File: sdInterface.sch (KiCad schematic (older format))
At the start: 3 parts, among them J1 SD_Card, J2 Conn_02x12_Counter_Clockwise

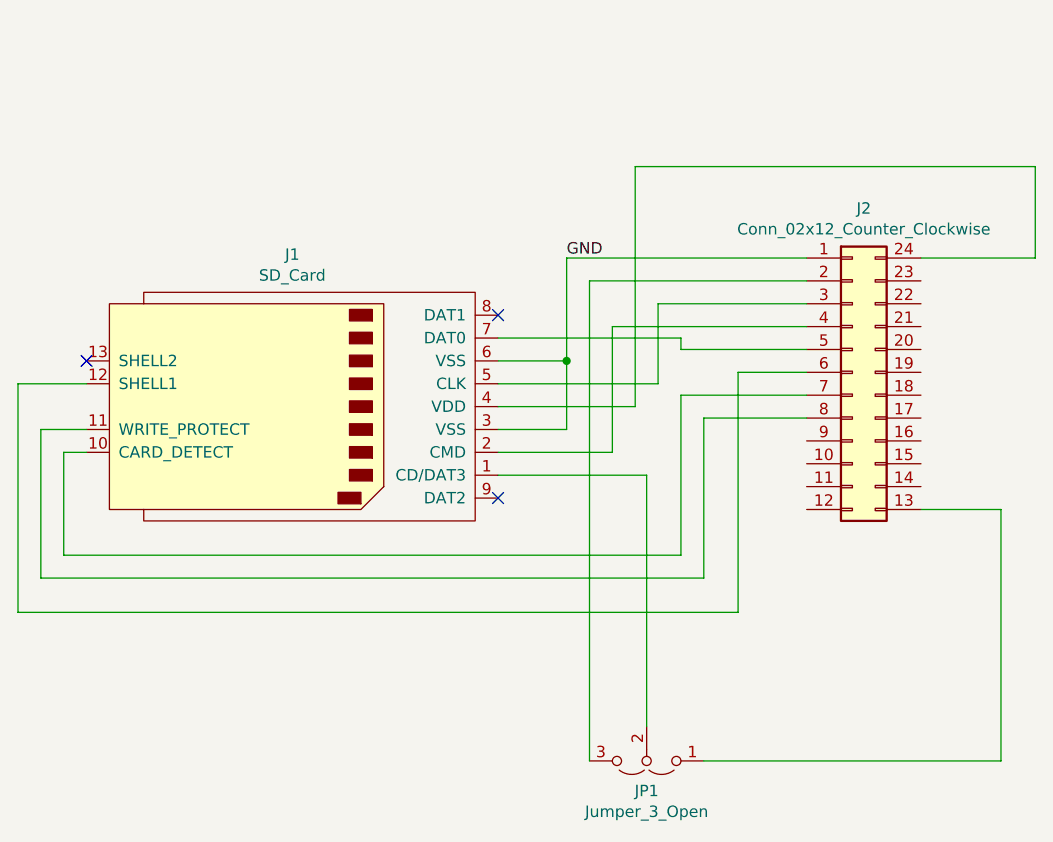
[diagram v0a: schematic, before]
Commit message: Added 3.3v reg, JP1 now pins
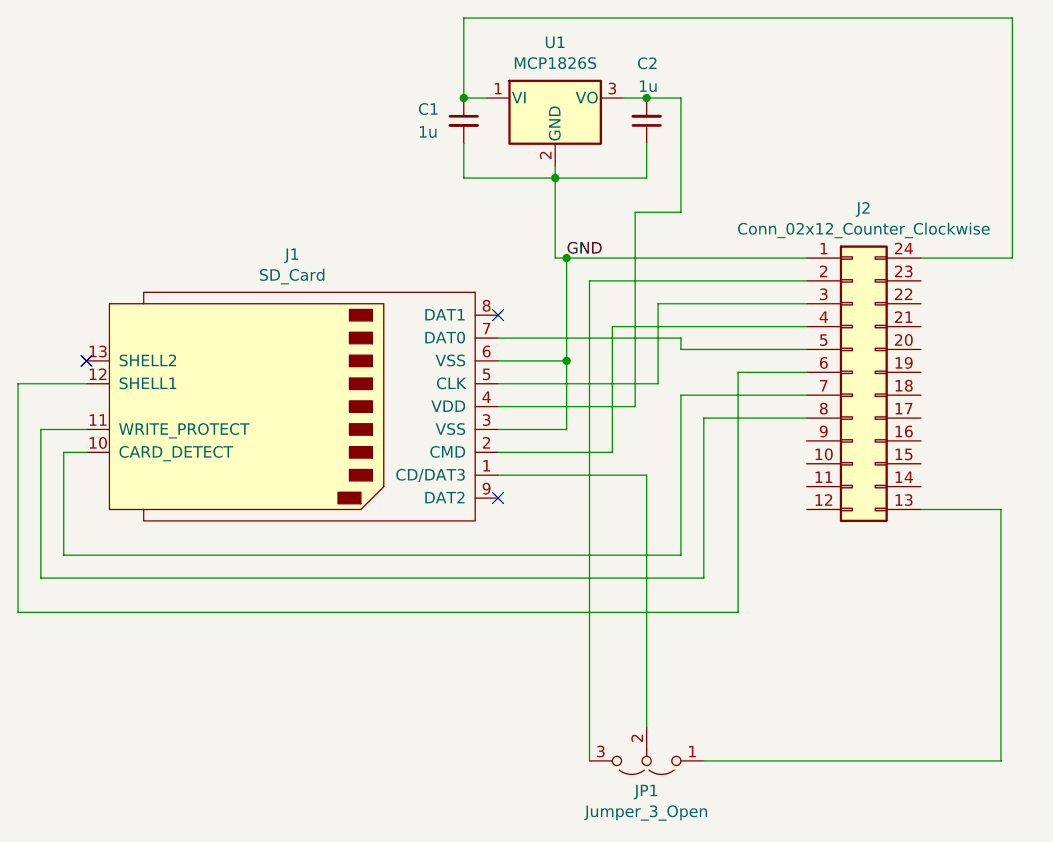
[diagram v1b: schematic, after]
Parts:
- added C1, C2: 1u, Capacitor_SMD:C_0805_2012Metric_Pad1.15x1.40mm_HandSolder, symbol Device:C_Small
- added U1: MCP1826S, Package_TO_SOT_SMD:SOT-223-3_TabPin2, symbol Regulator_Linear:MCP1826S
- JP1: footprint Jumper:SolderJumper-3_P1.3mm_Open_RoundedPad1.0x1.5mm -> Connector_PinHeader_2.54mm:PinHeader_1x03_P2.54mm_Vertical
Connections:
- net GND: now also C1.2, C2.1, U1.2 (GND)
- net at J2.24 (Pin_24): now also C1.1, U1.1 (VI); no longer J1.4 (VDD)
- new net: C2.2, J1.4 (VDD), U1.3 (VO)
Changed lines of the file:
@@
 F 0 "JP1" H 6150 5231 50  0000 C CNN
 F 1 "Jumper_3_Open" H 6150 5322 50  0000 C CNN
-F 2 "Jumper:SolderJumper-3_P1.3mm_Open_RoundedPad1.0x1.5mm" H 6150 5100 50  0001 C CNN
+F 2 "Connector_PinHeader_2.54mm:PinHeader_1x03_P2.54mm_Vertical" H 6150 5100 50  0001 C CNN
 F 3 "~" H 6150 5100 50  0001 C CNN
 	1    6150 5100
@@
 Wire Wire Line
 	5500 3550 6100 3550
-Wire Wire Line
-	6100 3550 6100 2500
-Wire Wire Line
-	6100 2500 7850 2500
-Wire Wire Line
-	7850 2500 7850 2900
-Wire Wire Line
-	7850 2900 7350 2900
 Wire Wire Line
 	5500 3450 6200 3450
@@
 Text Label 5800 2900 0    50   ~ 0
 GND
+$Comp
+L Regulator_Linear:MCP1826S U1
+U 1 1 5E2BFAF6
+P 5750 2200
+F 0 "U1" H 5750 2442 50  0000 C CNN
+F 1 "MCP1826S" H 5750 2351 50  0000 C CNN
+F 2 "Package_TO_SOT_SMD:SOT-223-3_TabPin2" H 5650 2350 50  0001 C CNN
+F 3 "http://ww1.microchip.com/downloads/en/DeviceDoc/22057B.pdf" H 5750 2450 50  0001 C CNN
+	1    5750 2200
+	1    0    0    -1
+$EndComp
+Wire Wire Line
+	5750 2500 5750 2550
+Wire Wire Line
+	5750 2900 5800 2900
+Connection ~ 5800 2900
+Wire Wire Line
+	7750 1850 7750 2900
+Wire Wire Line
+	7750 2900 7350 2900
+$Comp
+L Device:C_Small C1
+U 1 1 5E2C5E59
+P 5350 2300
+F 0 "C1" H 5150 2350 50  0000 L CNN
+F 1 "1u" H 5150 2250 50  0000 L CNN
+F 2 "Capacitor_SMD:C_0805_2012Metric_Pad1.15x1.40mm_HandSolder" H 5350 2300 50  0001 C CNN
+F 3 "~" H 5350 2300 50  0001 C CNN
+	1    5350 2300
+	1    0    0    -1
+$EndComp
+$Comp
+L Device:C_Small C2
+U 1 1 5E2C7B61
+P 6150 2300
+F 0 "C2" H 6100 2050 50  0000 L CNN
+F 1 "1u" H 6100 2150 50  0000 L CNN
+F 2 "Capacitor_SMD:C_0805_2012Metric_Pad1.15x1.40mm_HandSolder" H 6150 2300 50  0001 C CNN
+F 3 "~" H 6150 2300 50  0001 C CNN
+	1    6150 2300
+	-1   0    0    1
+$EndComp
+Wire Wire Line
+	5450 2200 5350 2200
+Wire Wire Line
+	5350 2400 5350 2550
+Wire Wire Line
+	5350 2550 5750 2550
+Connection ~ 5750 2550
+Wire Wire Line
+	5750 2550 5750 2900
+Wire Wire Line
+	5350 2200 5350 1850
+Wire Wire Line
+	5350 1850 7750 1850
+Connection ~ 5350 2200
+Wire Wire Line
+	6050 2200 6150 2200
+Wire Wire Line
+	6150 2400 6150 2550
+Wire Wire Line
+	6150 2550 5750 2550
+Wire Wire Line
+	6100 2700 6100 3550
+Wire Wire Line
+	6150 2200 6300 2200
+Wire Wire Line
+	6300 2200 6300 2700
+Wire Wire Line
+	6300 2700 6100 2700
+Connection ~ 6150 2200
 $EndSCHEMATC
